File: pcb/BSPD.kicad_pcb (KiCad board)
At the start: 4 copper layers, 60 parts, among them J1 Conn_02x06_Counter_Clockwise, Q1 AO3400A, U1 MCP1703A-5002_SOT23, U2 LM339, U3 LM339, U4 74HC32, U5 74HC02

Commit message: Schematic/layout for new revision
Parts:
- added C16: 0.1uF, Capacitor_SMD:C_0402_1005Metric, F.Cu at (145.5, 130.8)
- added C17: 10uF, Capacitor_SMD:C_0805_2012Metric, F.Cu at (145.5, 134.6)
- added C18: 10uF, Capacitor_SMD:C_0805_2012Metric, F.Cu at (145.5, 127.0)
- added G***: LOGO, LOGO, B.Cu at (135.7, 120.3)
- added J2: Conn_02x06_Counter_Clockwise, Connector:DTF13-12Px, F.Cu at (123.9, 144.8)
- added R24: 10k, Resistor_SMD:R_0402_1005Metric, F.Cu at (139.1, 110.5)
- added R25: 10k, Resistor_SMD:R_0402_1005Metric, F.Cu at (122.0, 135.2)
- added R26: 10k, Resistor_SMD:R_0402_1005Metric, F.Cu at (122.0, 137.1)
- added R27: 10k, Resistor_SMD:R_0402_1005Metric, F.Cu at (122.0, 139.0)
- added U6: AMS1117-5.0, Package_TO_SOT_SMD:SOT-223-3_TabPin2, F.Cu at (151.8, 128.2)
- C1: value 100uF -> 0.1uF; footprint Capacitor_SMD:C_1206_3216Metric -> Capacitor_SMD:C_0402_1005Metric
- C10, C7, C8: value 0.1uF -> 1uF
- C12, C15: value 1uF -> 10uF; footprint Capacitor_SMD:C_0402_1005Metric -> Capacitor_SMD:C_0805_2012Metric
- C13: value 10uF -> 100uF; footprint Capacitor_SMD:C_0805_2012Metric -> Capacitor_SMD:C_1206_3216Metric
- C14: value 1uF -> 0.1uF
- C2, C6: value 10uF -> 0.1uF; footprint Capacitor_SMD:C_0805_2012Metric -> Capacitor_SMD:C_0402_1005Metric
- C9: value 0.1uF -> 10uF; footprint Capacitor_SMD:C_0402_1005Metric -> Capacitor_SMD:C_0805_2012Metric
- D1: value D_Schottky -> SP0502BAHT; footprint Diode_SMD:D_SOD-323 -> Package_TO_SOT_SMD:SOT-23
- D2: value SP0502BAHT -> Green; footprint Package_TO_SOT_SMD:SOT-23 -> LED_SMD:LED_0603_1608Metric
- D3: value Green -> Yellow
- D4: value Yellow -> Red
- D5: value Red -> D_Schottky; footprint LED_SMD:LED_0603_1608Metric -> Diode_SMD:D_SOD-323
- J1: value Conn_02x06_Counter_Clockwise -> Test header; footprint Connector:DTF13-12Px -> Connector_PinHeader_2.54mm:PinHeader_2x14_P2.54mm_Vertical
- JP1: moved to F.Cu
- R10, R11, R12: value 1k -> 10k
- R13: value 100k -> 10k
- R14, R15, R16: value 100k -> 1k
- R17, R18: value 1k -> 100k
- R19, R20: value 10k -> 100k
- R21, R22, R5, R6, R7, R8: value 10k -> 1k
- U1: value MCP1703A-5002_SOT23 -> LM339; footprint Package_TO_SOT_SMD:SOT-23 -> Package_SO:SOIC-14_3.9x8.7mm_P1.27mm
- U3: value LM339 -> 74HC32
- U4: value 74HC32 -> 74HC02
- U5: value 74HC02 -> AMS1117-5.0; footprint Package_SO:SOIC-14_3.9x8.7mm_P1.27mm -> Package_TO_SOT_SMD:SOT-223-3_TabPin2
- moved R7 92.1 mm to (131.5, 140.9), turned to 90 degrees
- moved R5 84.3 mm to (123.9, 140.9), turned to 90 degrees
- moved C13 82.2 mm to (142.9, 139.7), turned to -90 degrees
- moved R6 81.7 mm to (129.0, 140.9)
- moved C14 81.2 mm to (145.5, 138.4), turned to 90 degrees
- moved C12 76.8 mm to (142.9, 134.6), turned to 90 degrees
- moved U5 76.3 mm to (151.8, 135.9), turned to 0 degrees
- moved R8 74.6 mm to (126.4, 140.9), turned to 90 degrees
- moved R19 72.4 mm to (125.2, 127.0)
- moved R15 72.3 mm to (154.9, 119.2)
- moved C9 70.7 mm to (125.2, 123.2), turned to 90 degrees
- moved R13 70.1 mm to (129.0, 129.5), turned to 180 degrees
- moved D5 69.9 mm to (129.6, 137.8), turned to -90 degrees
- moved C8 69.7 mm to (115.0, 114.9), turned to 180 degrees
- moved R14 67.7 mm to (154.9, 122.4)
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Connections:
- C1 pad 1: +12V -> BSE_in
- C10 pad 1: +5V -> /Sensor Pre-Delay
- C11 pad 1: Net-(C11-Pad1) -> +5V
- C11 pad 2: Startup -> Net-(C11-Pad2)
- C12 pad 1: Net-(C12-Pad1) -> +12V
- C13 pad 1: /Value Pre-Delay -> +12V
- C14 pad 1: /Sensor Pre-Delay -> +12V
- C15 pad 1: +5V -> +12V
- C15 pad 2: Net-(C15-Pad2) -> GND
- C2 pad 1: +12V -> TPS_in
- C3 pad 1: BSE_in -> +5V
- C4 pad 1: TPS_in -> +5V
- C5 pad 1: +12V -> +5V
- C7 pad 1: +5V -> Startup button
- C7 pad 2: GND -> Startup
- C8 pad 1: +5V -> Startup timer
- C9 pad 1: +5V -> /Value Pre-Delay
- D1 pad 1: +12V -> BSE_in
- D1 pad 2: Vin -> TPS_in
- D2 pad 1: BSE_in -> Net-(D2-Pad1)
- D2 pad 2: TPS_in -> +5V
- D3 pad 2: +5V -> Post-Delay
- D4 pad 2: Post-Delay -> FAULT_INV
- D5 pad 1: Net-(D5-Pad1) -> +12V
- D5 pad 2: FAULT_INV -> FAULT_12V
- D6 pad 2: FAULT_12V -> Vin
- J1 pad 1: Startup -> +5V
- J1 pad 10: FAULT_12V -> GND
- J1 pad 11: FAULT_5V -> TPS Error
- J1 pad 12: FAULT_3V3 -> GND
- J1 pad 2: Sensor Error -> GND
- J1 pad 3: Value Error -> Startup timer
- J1 pad 4: +5V -> GND
- J1 pad 5: Vin -> Startup button
- J1 pad 7: GND -> /Startup post-delay
- J1 pad 8: BSE_in -> GND
- J1 pad 9: TPS_in -> BSE Error
- R10 pad 1: GND -> Net-(R10-Pad1)
- R10 pad 2: Net-(D3-Pad1) -> +5V
- R11 pad 1: GND -> Value Error
- R11 pad 2: Net-(D4-Pad1) -> +5V
- R12 pad 1: GND -> Net-(R12-Pad1)
- R12 pad 2: Net-(D5-Pad1) -> +5V
- R13 pad 1: +5V -> Net-(R13-Pad1)
- R13 pad 2: Net-(C11-Pad1) -> +5V
- R14 pad 1: +5V -> GND
- R14 pad 2: Net-(C12-Pad1) -> Net-(D2-Pad1)
- R15 pad 1: Value Error -> GND
- R15 pad 2: /Value Pre-Delay -> Net-(D3-Pad1)
- R16 pad 1: Sensor Error -> GND
- R16 pad 2: /Sensor Pre-Delay -> Net-(D4-Pad1)
- R17 pad 1: FAULT_5V -> +5V
- R17 pad 2: Net-(Q1-Pad1) -> Startup button
- R18 pad 1: FAULT_INV -> +5V
- R18 pad 2: Net-(C15-Pad2) -> Startup timer
- R19 pad 1: /Value Post-Delay -> Value Error
- R19 pad 2: +5V -> /Value Pre-Delay
- R20 pad 1: /Sensor Post-Delay -> Sensor Error
- R20 pad 2: +5V -> /Sensor Pre-Delay
- R21 pad 1: FAULT_3V3 -> FAULT_5V
- R21 pad 2: FAULT_5V -> Net-(Q1-Pad1)
- R22 pad 1: FAULT_3V3 -> FAULT_INV
- R22 pad 2: Net-(R22-Pad2) -> Net-(C11-Pad2)
- R23 pad 1: Net-(R22-Pad2) -> /Value Post-Delay
- R23 pad 2: GND -> +5V
- R5 pad 1: Net-(R5-Pad1) -> Net-(J2-Pad1)
- R5 pad 2: +5V -> Startup
- R6 pad 1: Net-(R6-Pad1) -> Net-(J2-Pad2)
- R6 pad 2: +5V -> Sensor Error
- R7 pad 1: Value Error -> Net-(J2-Pad3)
- R7 pad 2: +5V -> Value Error
- R8 pad 1: Net-(R8-Pad1) -> Net-(J2-Pad11)
- R8 pad 2: +5V -> FAULT_5V
- U1 pad 1: GND -> Net-(R10-Pad1)
- U1 pad 2: +5V -> Net-(R9-Pad1)
- U1 pad 3: +12V -> +5V
- U2 pad 1: Net-(R6-Pad1) -> Value Error
- U2 pad 10: TPS_HIGH -> VALUE_DELAY
- U2 pad 11: TPS_in -> /Value Pre-Delay
- U2 pad 13: Net-(R8-Pad1) -> /Value Post-Delay
- U2 pad 14: Net-(R9-Pad1) -> /Sensor Post-Delay
- U2 pad 2: Net-(R5-Pad1) -> Value Error
- U2 pad 4: BSE_HIGH -> BSE_THRESH
- U2 pad 6: BSE_in -> TPS_THRESH
- U2 pad 7: BSE_LOW -> TPS_in
- U2 pad 8: TPS_in -> SENSOR_DELAY
- U2 pad 9: TPS_LOW -> /Sensor Pre-Delay
- U3 pad 1: Value Error -> Net-(R9-Pad1)
- U3 pad 10: VALUE_DELAY -> TPS Error
- U3 pad 11: /Value Pre-Delay -> Post-Delay
- U3 pad 12: GND -> /Value Post-Delay
- U3 pad 13: /Value Post-Delay -> /Sensor Post-Delay
- U3 pad 14: /Sensor Post-Delay -> +5V
- U3 pad 2: Value Error -> Net-(R10-Pad1)
- U3 pad 3: +5V -> BSE Error
- U3 pad 4: BSE_THRESH -> Net-(R12-Pad1)
- U3 pad 5: BSE_in -> Net-(R13-Pad1)
- U3 pad 6: TPS_THRESH -> TPS Error
- U3 pad 7: TPS_in -> GND
- U3 pad 8: SENSOR_DELAY -> Sensor Error
- U3 pad 9: /Sensor Pre-Delay -> BSE Error
- U4 pad 1: Net-(R5-Pad1) -> FAULT_5V
- U4 pad 10: Net-(TP5-Pad1) -> /Startup post-delay
- U4 pad 11: Post-Delay -> (no net)
- U4 pad 12: /Value Post-Delay -> (no net)
- U4 pad 13: /Sensor Post-Delay -> (no net)
- U4 pad 2: Net-(R6-Pad1) -> Post-Delay
- U4 pad 3: Net-(TP4-Pad1) -> Net-(C11-Pad2)
- U4 pad 4: Net-(R8-Pad1) -> FAULT_INV
- U4 pad 5: Net-(R9-Pad1) -> FAULT_5V
- U4 pad 6: Net-(TP5-Pad1) -> /Startup post-delay
- U4 pad 8: Sensor Error -> Startup button
- U4 pad 9: Net-(TP4-Pad1) -> Startup timer
- U5 pad 1: FAULT_5V -> GND
- U5 pad 2: Post-Delay -> +5VE
- U5 pad 3: Net-(C15-Pad2) -> +12V
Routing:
- net FAULT_5V: track 30.7 -> 88.2 mm, vias 0 -> 4
- net /Sensor Pre-Delay: track 3.72 -> 59.0 mm, vias 0 -> 3
- net /Value Pre-Delay: track 12.7 -> 65.7 mm
- net TPS_THRESH: track 5.42 -> 52.1 mm, vias 0 -> 2
- net /Value Post-Delay: track 23.7 -> 70.4 mm, vias 2 -> 3
- net /Sensor Post-Delay: track 25.9 -> 70.0 mm, vias 2 -> 3
- net TPS Error: track 0.00 -> 37.2 mm, vias 0 -> 1
- net Startup timer: track 0.00 -> 36.7 mm, vias 0 -> 1
- net Value Error: track 44.6 -> 79.3 mm, vias 1 -> 4
- net BSE Error: track 0.00 -> 34.0 mm, vias 0 -> 1
- net Net-(R5-Pad1): track 31.8 -> 0.00 mm
- net Startup: track 23.4 -> 55.0 mm, vias 1 -> 3
- net Post-Delay: track 33.6 -> 65.1 mm
- net /Startup post-delay: track 0.00 -> 30.8 mm, vias 0 -> 1
- net Startup button: track 0.00 -> 29.0 mm
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- added copper zone on In2.Cu, net +5VE
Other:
- board outline added: 45 x 70 mm
- board text added: "+5V Start Timer Start Btn Start Post BSE Error TPS Error Sensor Err Sensor Pre Sensor Post Value Error Value Pre Value Post Post-Delay Fault-5V"
- board text added: "BSE"
- board text added: "Bronco Racing BSPD Rev. 5"
- board text added: "DIDN'T EVEN KNOW THEY WERE CATHOLIC"
- board text added: "Delay"
- board text added: "High Low Thresh"
- board text added: "JUST FOUND OUT THAT ELECTRONS HAVE MASS."
- board text added: "Jack LeFevre Oct 2022"
- board text added: "Startup"
- board text added: "TPS"
- board text added: "Value Sensor"

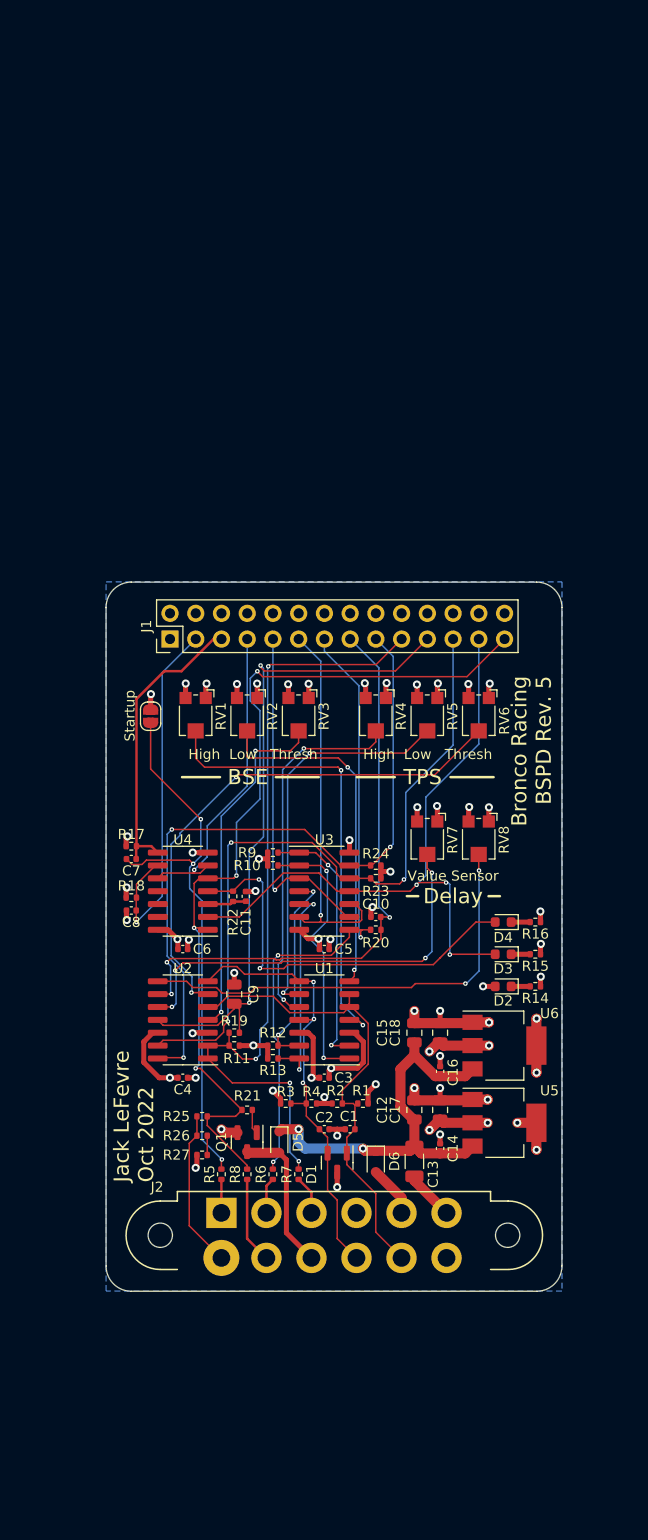
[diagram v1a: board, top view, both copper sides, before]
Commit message: Switched to vertical DTM header
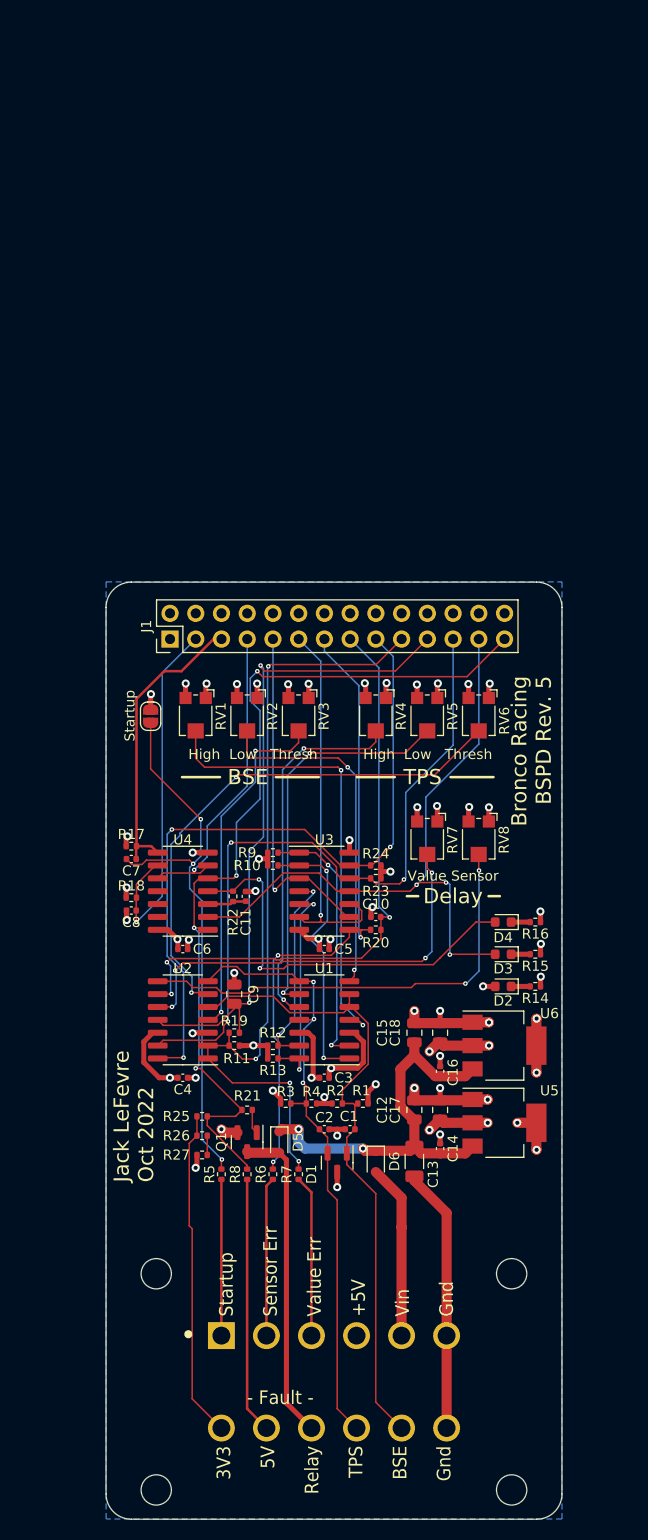
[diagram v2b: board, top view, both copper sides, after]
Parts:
- J2: footprint Connector:DTF13-12Px -> libraries:TE_DT15-12PA
- moved J2 20.0 mm to (135.0, 161.4), turned to -90 degrees
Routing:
- net GND: track 73.6 -> 94.8 mm
- net TPS_in: track 44.6 -> 61.4 mm
- net BSE_in: track 46.1 -> 62.9 mm
- net FAULT_3V3: track 15.6 -> 32.4 mm
- net Net-(J2-Pad11): track 8.53 -> 25.3 mm
- net FAULT_12V: track 14.9 -> 31.7 mm
- net Vin: track 5.08 -> 17.2 mm
- net Net-(J2-Pad3): track 3.83 -> 15.9 mm
- net Net-(J2-Pad2): track 3.56 -> 15.7 mm
- net Net-(J2-Pad1): track 3.30 -> 15.4 mm
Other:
- board size 45 x 70 mm -> 45 x 92.5 mm
- board text added: "- Fault -"
- board text added: "3V3 5V Relay TPS BSE Gnd"
- board text added: "Startup Sensor Err Value Err +5V Vin Gnd"

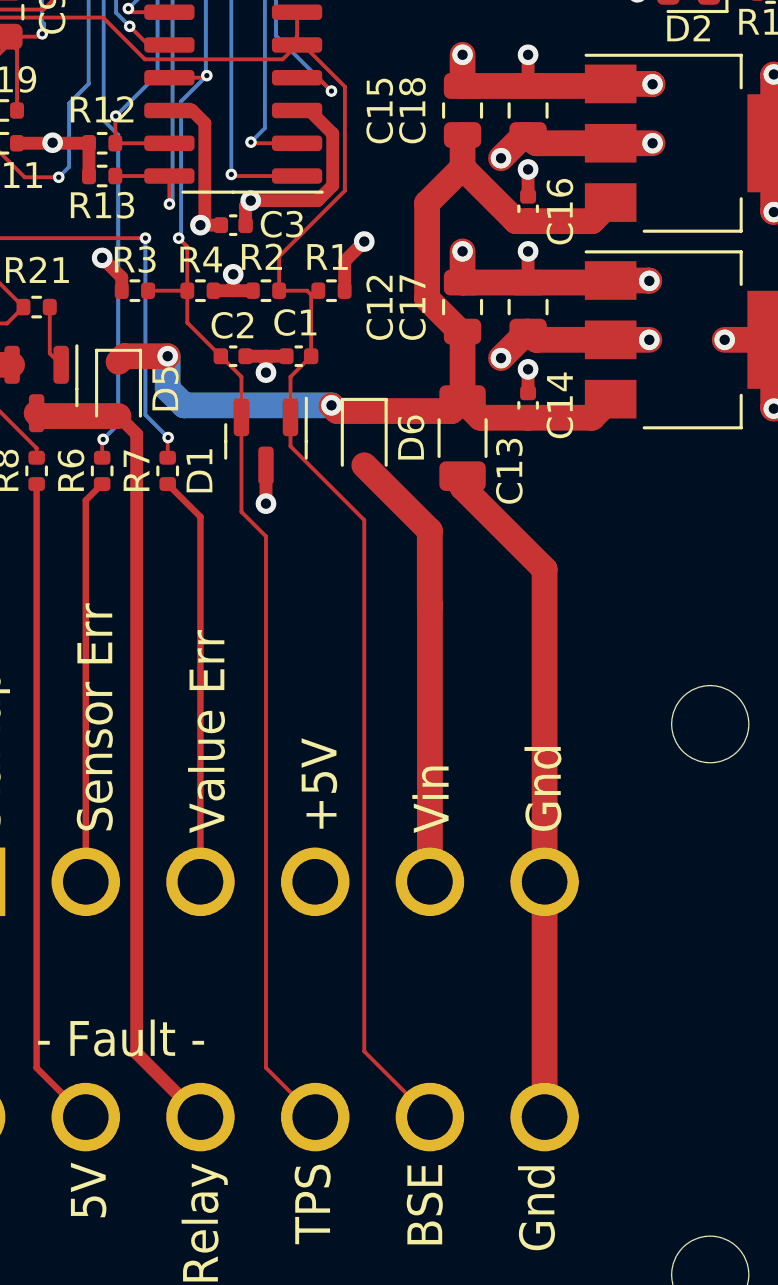
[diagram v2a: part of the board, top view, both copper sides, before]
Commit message: Fixed flyback/reverse polarity protection, added part #s
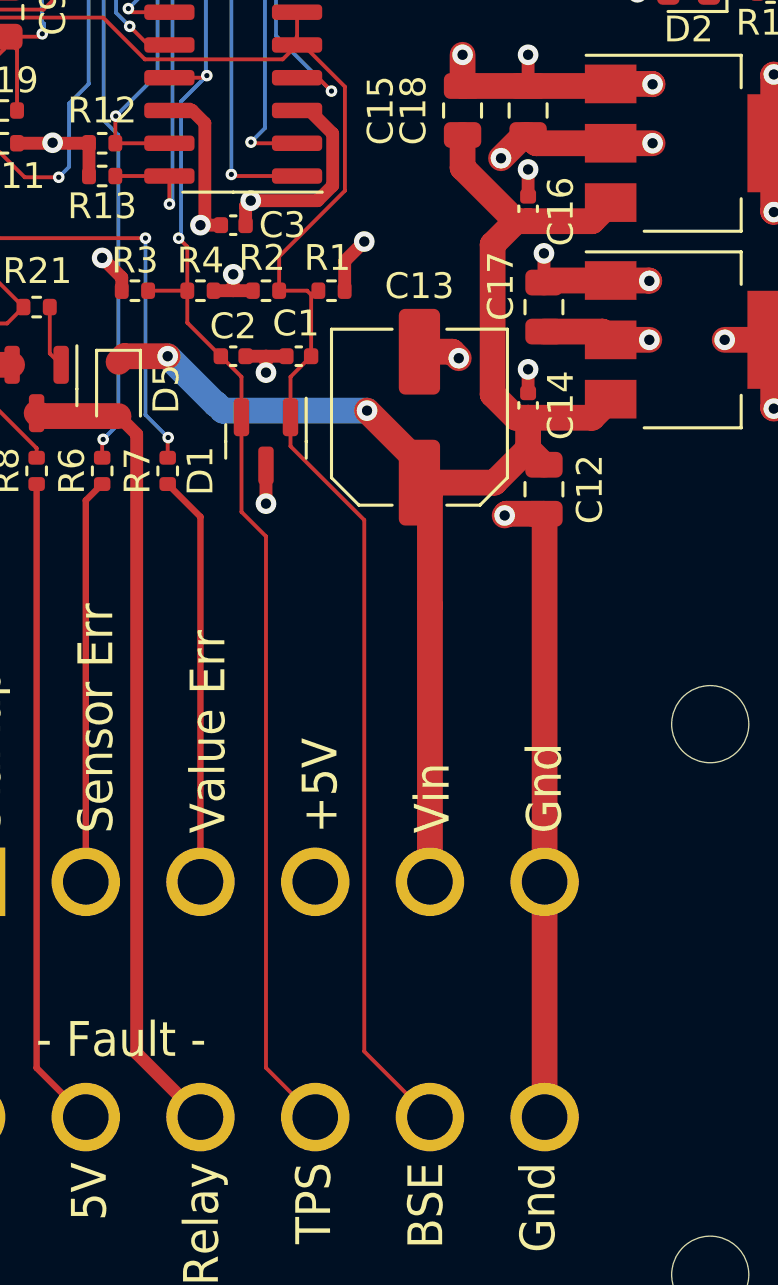
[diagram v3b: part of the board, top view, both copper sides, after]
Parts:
- removed D6: D_Schottky, Diode_SMD:D_SOD-323
- C13: footprint Capacitor_SMD:C_1206_3216Metric -> Capacitor_SMD:C_Elec_6.3x7.7
- D4: value Red -> Blue
- moved C12 7.73 mm to (146.1, 141.7), turned to -90 degrees
- moved C13 1.86 mm to (141.3, 138.9), turned to 90 degrees
- moved C17 0.62 mm to (146.1, 134.6)
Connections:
- C12 pad 1: +12V -> Vin
- C13 pad 1: +12V -> Vin
- C14 pad 1: +12V -> Vin
- C15 pad 1: +12V -> Vin
- C16 pad 1: +12V -> Vin
- D5 pad 1: +12V -> Vin
- U5 pad 3: +12V -> Vin
- U6 pad 3: +12V -> Vin
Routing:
- net Vin: track 17.2 -> 57.2 mm, vias 0 -> 2
- net +12V: track 39.8 -> 0.00 mm, vias 2 -> 0
- net GND: track 94.8 -> 90.9 mm, vias 33 -> 34
- net +5VE: track 10.8 -> 8.77 mm, vias 4 -> 3
